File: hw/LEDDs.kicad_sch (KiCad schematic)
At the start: 3 parts

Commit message: Update design
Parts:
- H1, H2, H3: value mounting hole -> 20mm
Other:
- moved on the sheet: H1, H2, H3
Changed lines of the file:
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@@
 (kicad_sch
-	(version 20231120)
+	(version 20250114)
 	(generator "eeschema")
-	(generator_version "8.0")
+	(generator_version "9.0")
 	(paper "A4")
 	(title_block
 		(title "LEDDs")
-		(date "2025-02-17")
-		(rev "1.0")
+		(date "2025-04-02")
+		(rev "2.0")
 		(company "Vas's lab")
 	)
@@
 	(symbol
 		(lib_id "Mechanical:MountingHole")
-		(at 158.75 180.34 0)
+		(at 166.37 180.34 0)
 		(unit 1)
 		(exclude_from_sim yes)
@@
 		(dnp no)
 		(property "Reference" "H1"
-			(at 161.036 179.07 0)
-			(effects
-				(font
-					(size 1.27 1.27)
-				)
-				(justify left)
-			)
-		)
-		(property "Value" "mounting hole"
-			(at 161.036 181.61 0)
+			(at 168.656 179.07 0)
+			(effects
+				(font
+					(size 1.27 1.27)
+				)
+				(justify left)
+			)
+		)
+		(property "Value" "20mm"
+			(at 168.656 181.61 0)
 			(effects
 				(font
@@
 		)
 		(property "Footprint" "MountingHole:MountingHole_3.2mm_M3_DIN965_Pad_TopBottom"
-			(at 158.75 180.34 0)
+			(at 166.37 180.34 0)
 			(effects
 				(font
@@
 		)
 		(property "Datasheet" "~"
-			(at 158.75 180.34 0)
-			(effects
-				(font
-					(size 1.27 1.27)
-				)
-				(hide yes)
-			)
-		)
-		(property "Description" "M3"
-			(at 158.75 180.34 0)
+			(at 166.37 180.34 0)
+			(effects
+				(font
+					(size 1.27 1.27)
+				)
+				(hide yes)
+			)
+		)
+		(property "Description" "M3x20mm"
+			(at 166.37 180.34 0)
 			(effects
 				(font
@@
 	(symbol
 		(lib_id "Mechanical:MountingHole")
-		(at 158.75 193.04 0)
+		(at 166.37 193.04 0)
 		(unit 1)
 		(exclude_from_sim yes)
@@
 		(dnp no)
 		(property "Reference" "H3"
-			(at 161.036 191.7699 0)
-			(effects
-				(font
-					(size 1.27 1.27)
-				)
-				(justify left)
-			)
-		)
-		(property "Value" "mounting hole"
-			(at 161.036 194.3099 0)
+			(at 168.656 191.7699 0)
+			(effects
+				(font
+					(size 1.27 1.27)
+				)
+				(justify left)
+			)
+		)
+		(property "Value" "20mm"
+			(at 168.656 194.3099 0)
 			(effects
 				(font
@@
 		)
 		(property "Footprint" "MountingHole:MountingHole_3.2mm_M3_DIN965_Pad_TopBottom"
-			(at 158.75 193.04 0)
+			(at 166.37 193.04 0)
 			(effects
 				(font
@@
 		)
 		(property "Datasheet" "~"
-			(at 158.75 193.04 0)
-			(effects
-				(font
-					(size 1.27 1.27)
-				)
-				(hide yes)
-			)
-		)
-		(property "Description" "M3"
-			(at 158.75 193.04 0)
+			(at 166.37 193.04 0)
+			(effects
+				(font
+					(size 1.27 1.27)
+				)
+				(hide yes)
+			)
+		)
+		(property "Description" "M3x20mm"
+			(at 166.37 193.04 0)
 			(effects
 				(font
@@
 	(symbol
 		(lib_id "Mechanical:MountingHole")
-		(at 158.75 186.69 0)
+		(at 166.37 186.69 0)
 		(unit 1)
 		(exclude_from_sim yes)
@@
 		(dnp no)
 		(property "Reference" "H2"
-			(at 161.036 185.42 0)
-			(effects
-				(font
-					(size 1.27 1.27)
-				)
-				(justify left)
-			)
-		)
-		(property "Value" "mounting hole"
-			(at 161.036 187.96 0)
+			(at 168.656 185.42 0)
+			(effects
+				(font
+					(size 1.27 1.27)
+				)
+				(justify left)
+			)
+		)
+		(property "Value" "20mm"
+			(at 168.656 187.96 0)
 			(effects
 				(font
@@
 		)
 		(property "Footprint" "MountingHole:MountingHole_3.2mm_M3_DIN965_Pad_TopBottom"
-			(at 158.75 186.69 0)
+			(at 166.37 186.69 0)
 			(effects
 				(font
@@
 		)
 		(property "Datasheet" "~"
-			(at 158.75 186.69 0)
-			(effects
-				(font
-					(size 1.27 1.27)
-				)
-				(hide yes)
-			)
-		)
-		(property "Description" "M3"
-			(at 158.75 186.69 0)
+			(at 166.37 186.69 0)
+			(effects
+				(font
+					(size 1.27 1.27)
+				)
+				(hide yes)
+			)
+		)
+		(property "Description" "M3x20mm"
+			(at 166.37 186.69 0)
 			(effects
 				(font
@@
 		(at 140.97 86.36)
 		(size 20.32 20.32)
+		(exclude_from_sim no)
+		(in_bom yes)
+		(on_board yes)
+		(dnp no)
 		(fields_autoplaced yes)
 		(stroke
@@
 	(sheet
 		(at 163.83 86.36)
-		(size 22.86 20.32)
+		(size 20.32 20.32)
+		(exclude_from_sim no)
+		(in_bom yes)
+		(on_board yes)
+		(dnp no)
 		(fields_autoplaced yes)
 		(stroke
@@
 	)
 	(sheet
-		(at 119.38 86.36)
-		(size 19.05 20.32)
+		(at 118.11 86.36)
+		(size 20.32 20.32)
+		(exclude_from_sim no)
+		(in_bom yes)
+		(on_board yes)
+		(dnp no)
 		(fields_autoplaced yes)
 		(stroke
@@
 		)
 		(property "Sheetname" "Power"
-			(at 119.38 85.6484 0)
+			(at 118.11 85.6484 0)
 			(effects
 				(font
@@
 		)
 		(property "Sheetfile" "pwr.kicad_sch"
-			(at 119.38 107.2646 0)
+			(at 118.11 107.2646 0)
 			(effects
 				(font
@@
 		)
 	)
+	(embedded_fonts no)
 )

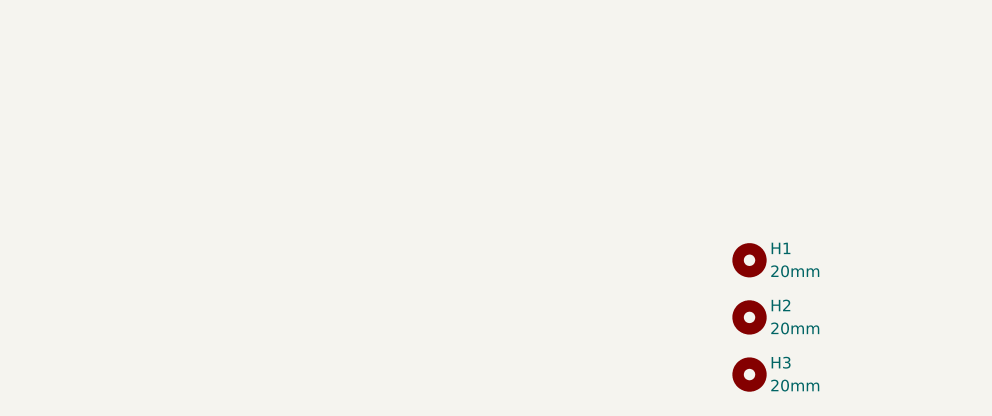
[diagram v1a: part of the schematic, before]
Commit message: Fix included libraries. Arrange schematic notes. Add mechanical parts to schematic.
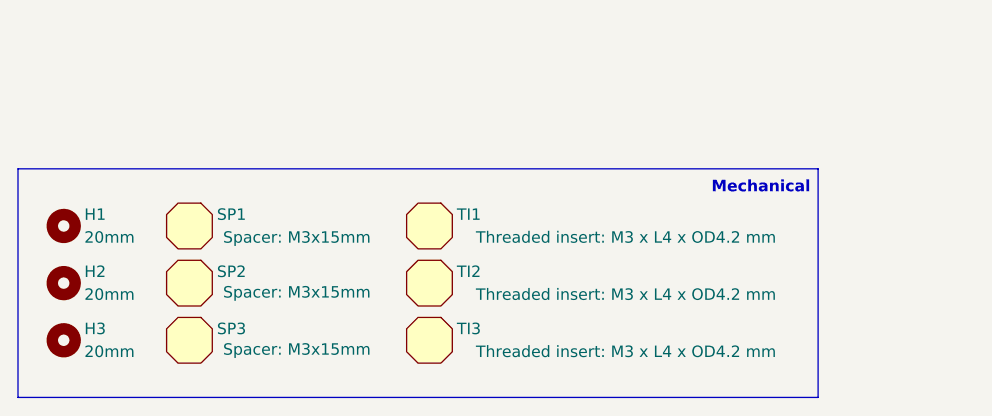
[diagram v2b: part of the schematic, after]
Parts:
- added SP1, SP2, SP3: 15mm, symbol Mechanical:Mechanical_Shape
- added TI1, TI2, TI3: 4x4.2 mm, symbol Mechanical:Mechanical_Shape
- H1, H2, H3: now in the parts list
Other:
- moved on the sheet: H1, H2, H3
